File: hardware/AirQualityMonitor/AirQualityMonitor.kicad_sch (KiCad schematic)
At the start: 0 parts

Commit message: Add USB C connector with CC pulldowns and data pin pairing
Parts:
- added J1: USB_C_Receptacle_USB2.0_16P, Connector_USB:USB_C_Receptacle_HRO_TYPE-C-31-M-12, symbol Connector:USB_C_Receptacle_USB2.0_16P
- added R1, R2: 5100, Resistor_SMD:R_0603_1608Metric, symbol Device:R
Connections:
- new net: J1.B5 (CC2), R1.1
- new net: J1.A5 (CC1), R2.1
- new net: J1.A4 (VBUS), J1.A9 (VBUS), J1.B4 (VBUS), J1.B9 (VBUS)
- new net: J1.A6 (D+), J1.B6 (D+)
- new net: J1.A7 (D-), J1.B7 (D-)
- new net GND: J1.A1 (GND), J1.A12 (GND), J1.B1 (GND), J1.B12 (GND), J1.SH (SHIELD), R1.2, R2.2
- no-connect marks 0 -> 2
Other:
- title: (none) -> Air Quality Monitor

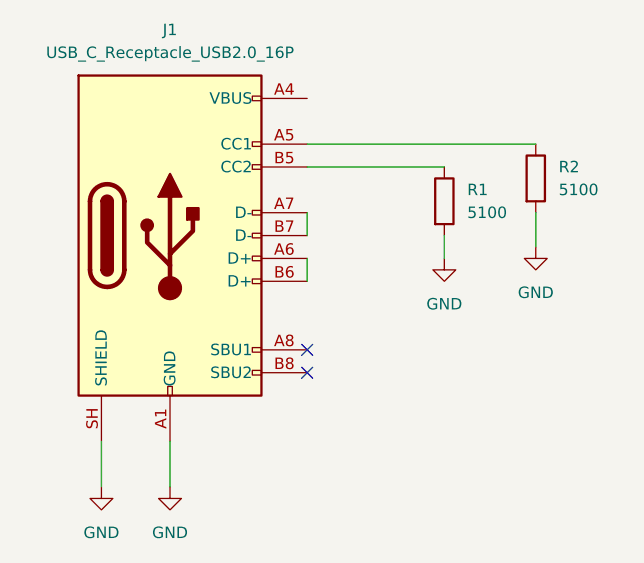
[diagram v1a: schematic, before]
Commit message: Add VBUS fuse and 5V rail
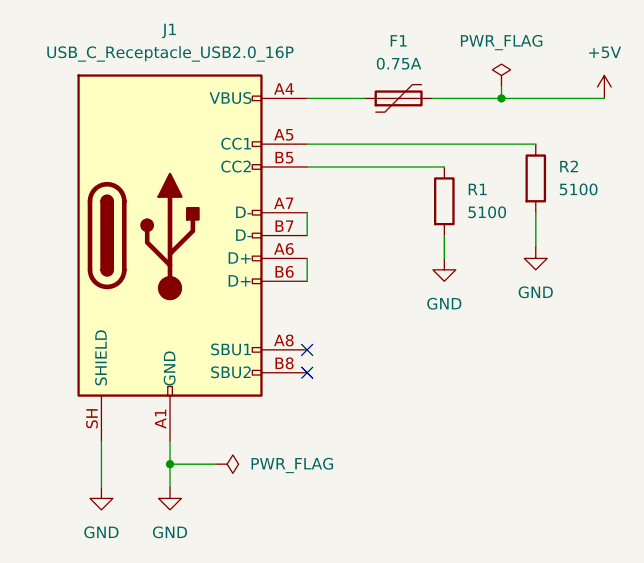
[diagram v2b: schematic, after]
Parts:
- added F1: 0.75A, Fuse:Fuse_1206_3216Metric, symbol Device:Polyfuse
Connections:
- net at J1.A4 (VBUS), J1.A9 (VBUS), J1.B4 (VBUS)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: now also F1.1
- new net +5V: F1.2

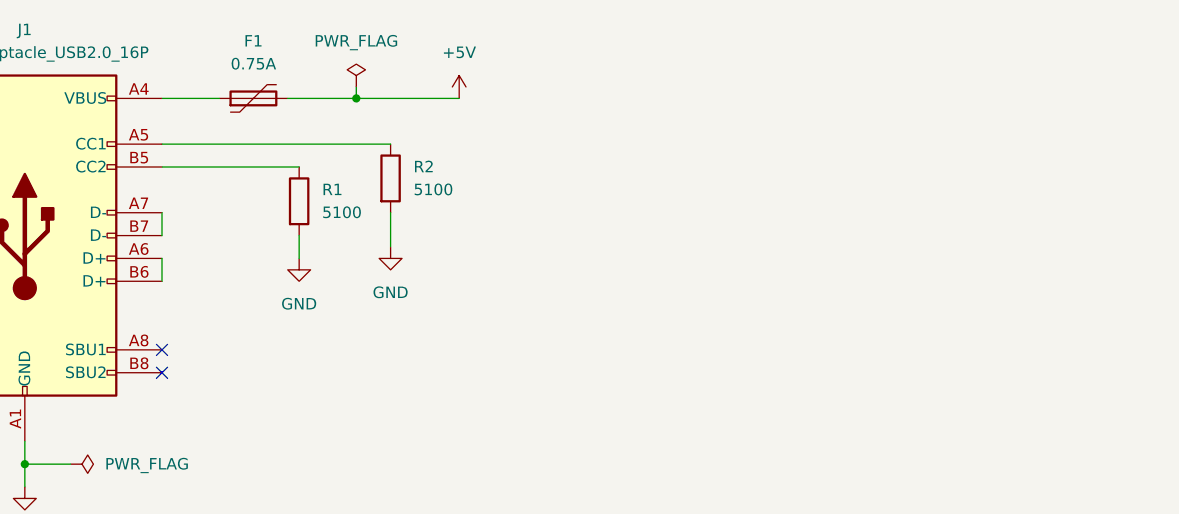
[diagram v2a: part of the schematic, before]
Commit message: Add USB ESD protection and USB data net labels
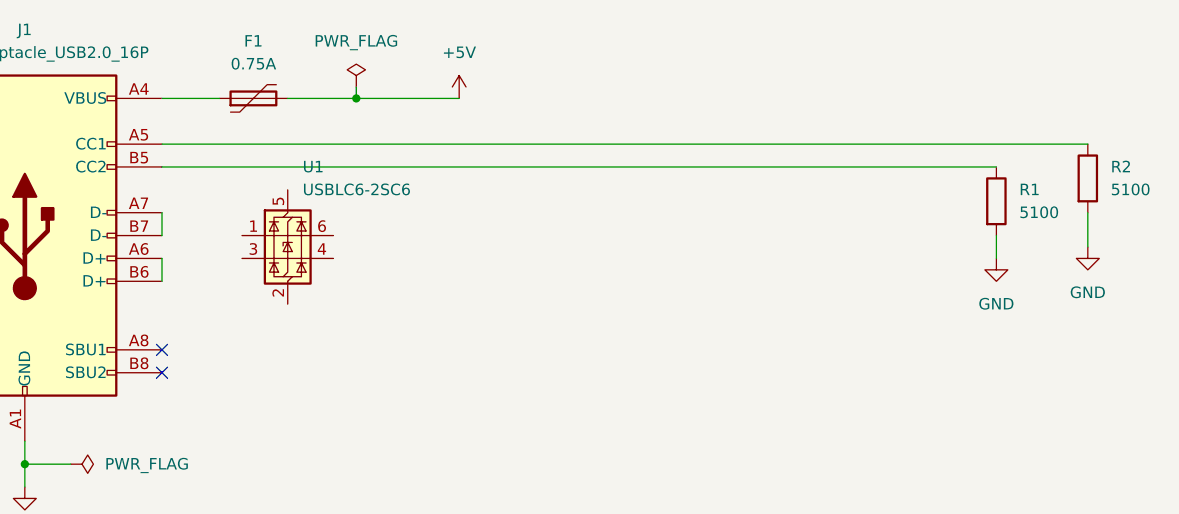
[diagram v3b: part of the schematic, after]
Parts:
- added U1: USBLC6-2SC6, Package_TO_SOT_SMD:SOT-23-6, symbol Power_Protection:USBLC6-2SC6
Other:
- moved on the sheet: R1, R2
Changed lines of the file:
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@@
 	(wire
 		(pts
-			(xy 88.9 100.33) (xy 88.9 104.14)
+			(xy 166.37 100.33) (xy 166.37 104.14)
 		)
 		(stroke
@@
 	(wire
 		(pts
-			(xy 78.74 102.87) (xy 78.74 105.41)
+			(xy 156.21 102.87) (xy 156.21 105.41)
 		)
 		(stroke
@@
 	(wire
 		(pts
-			(xy 63.5 92.71) (xy 88.9 92.71)
+			(xy 63.5 92.71) (xy 166.37 92.71)
 		)
 		(stroke
@@
 	(wire
 		(pts
-			(xy 63.5 95.25) (xy 78.74 95.25)
+			(xy 63.5 105.41) (xy 63.5 107.95)
 		)
 		(stroke
@@
 	(wire
 		(pts
-			(xy 63.5 105.41) (xy 63.5 107.95)
+			(xy 85.09 86.36) (xy 85.09 87.63)
 		)
 		(stroke
@@
 	(wire
 		(pts
-			(xy 85.09 86.36) (xy 85.09 87.63)
+			(xy 63.5 95.25) (xy 156.21 95.25)
 		)
 		(stroke
@@
 	(symbol
 		(lib_id "Device:R")
-		(at 78.74 99.06 0)
+		(at 156.21 99.06 0)
 		(unit 1)
 		(body_style 1)
@@
 		(fields_autoplaced yes)
 		(property "Reference" "R1"
-			(at 81.28 97.7899 0)
+			(at 158.75 97.7899 0)
 			(show_name no)
 			(do_not_autoplace no)
@@
 		)
 		(property "Value" "5100"
-			(at 81.28 100.3299 0)
+			(at 158.75 100.3299 0)
 			(show_name no)
 			(do_not_autoplace no)
@@
 		)
 		(property "Footprint" "Resistor_SMD:R_0603_1608Metric"
-			(at 76.962 99.06 90)
+			(at 154.432 99.06 90)
 			(hide yes)
 			(show_name no)
@@
 		)
 		(property "Datasheet" ""
-			(at 78.74 99.06 0)
+			(at 156.21 99.06 0)
 			(hide yes)
 			(show_name no)
@@
 		)
 		(property "Description" "Resistor"
-			(at 78.74 99.06 0)
+			(at 156.21 99.06 0)
 			(hide yes)
 			(show_name no)
@@
 	(symbol
 		(lib_id "power:GND")
-		(at 78.74 105.41 0)
+		(at 156.21 105.41 0)
 		(unit 1)
 		(body_style 1)
@@
 		(fields_autoplaced yes)
 		(property "Reference" "#PWR01"
-			(at 78.74 111.76 0)
+			(at 156.21 111.76 0)
 			(hide yes)
 			(show_name no)
@@
 		)
 		(property "Value" "GND"
-			(at 78.74 110.49 0)
+			(at 156.21 110.49 0)
 			(show_name no)
 			(do_not_autoplace no)
@@
 		)
 		(property "Footprint" ""
-			(at 78.74 105.41 0)
+			(at 156.21 105.41 0)
 			(hide yes)
 			(show_name no)
@@
 		)
 		(property "Datasheet" ""
-			(at 78.74 105.41 0)
+			(at 156.21 105.41 0)
 			(hide yes)
 			(show_name no)
@@
 		)
 		(property "Description" "Power symbol creates a global label with name \"GND\" , ground"
-			(at 78.74 105.41 0)
+			(at 156.21 105.41 0)
 			(hide yes)
 			(show_name no)
@@
 	(symbol
 		(lib_id "Device:R")
-		(at 88.9 96.52 0)
+		(at 166.37 96.52 0)
 		(unit 1)
 		(body_style 1)
@@
 		(fields_autoplaced yes)
 		(property "Reference" "R2"
-			(at 91.44 95.2499 0)
+			(at 168.91 95.2499 0)
 			(show_name no)
 			(do_not_autoplace no)
@@
 		)
 		(property "Value" "5100"
-			(at 91.44 97.7899 0)
+			(at 168.91 97.7899 0)
 			(show_name no)
 			(do_not_autoplace no)
@@
 		)
 		(property "Footprint" "Resistor_SMD:R_0603_1608Metric"
-			(at 87.122 96.52 90)
+			(at 164.592 96.52 90)
 			(hide yes)
 			(show_name no)
@@
 		)
 		(property "Datasheet" ""
-			(at 88.9 96.52 0)
+			(at 166.37 96.52 0)
 			(hide yes)
 			(show_name no)
@@
 		)
 		(property "Description" "Resistor"
-			(at 88.9 96.52 0)
+			(at 166.37 96.52 0)
 			(hide yes)
 			(show_name no)
@@
 	(symbol
 		(lib_id "power:GND")
-		(at 88.9 104.14 0)
+		(at 166.37 104.14 0)
 		(unit 1)
 		(body_style 1)
@@
 		(fields_autoplaced yes)
 		(property "Reference" "#PWR02"
-			(at 88.9 110.49 0)
+			(at 166.37 110.49 0)
 			(hide yes)
 			(show_name no)
@@
 		)
 		(property "Value" "GND"
-			(at 88.9 109.22 0)
+			(at 166.37 109.22 0)
 			(show_name no)
 			(do_not_autoplace no)
@@
 		)
 		(property "Footprint" ""
-			(at 88.9 104.14 0)
+			(at 166.37 104.14 0)
 			(hide yes)
 			(show_name no)
@@
 		)
 		(property "Datasheet" ""
-			(at 88.9 104.14 0)
+			(at 166.37 104.14 0)
 			(hide yes)
 			(show_name no)
@@
 		)
 		(property "Description" "Power symbol creates a global label with name \"GND\" , ground"
-			(at 88.9 104.14 0)
+			(at 166.37 104.14 0)
 			(hide yes)
 			(show_name no)
@@
 					(unit 1)
 				)
+			)
+		)
+	)
+	(symbol
+		(lib_id "Power_Protection:USBLC6-2SC6")
+		(at 77.47 102.87 0)
+		(unit 1)
+		(body_style 1)
+		(exclude_from_sim no)
+		(in_bom yes)
+		(on_board yes)
+		(in_pos_files yes)
+		(dnp no)
+		(fields_autoplaced yes)
+		(property "Reference" "U1"
+			(at 79.1211 95.25 0)
+			(show_name no)
+			(do_not_autoplace no)
+			(effects
+				(font
+					(size 1.27 1.27)
+				)
+				(justify left)
+			)
+		)
+		(property "Value" "USBLC6-2SC6"
+			(at 79.1211 97.79 0)
+			(show_name no)
+			(do_not_autoplace no)
+			(effects
+				(font
+					(size 1.27 1.27)
+				)
+				(justify left)
+			)
+		)
+		(property "Footprint" "Package_TO_SOT_SMD:SOT-23-6"
+			(at 78.74 109.22 0)
+			(hide yes)
+			(show_name no)
+			(do_not_autoplace no)
+			(effects
+				(font
+					(size 1.27 1.27)
+					(italic yes)
+				)
+				(justify left)
+			)
+		)
+		(property "Datasheet" "https://www.st.com/resource/en/datasheet/usblc6-2.pdf"
+			(at 78.74 111.125 0)
+			(hide yes)
+			(show_name no)
+			(do_not_autoplace no)
+			(effects
+				(font
+					(size 1.27 1.27)
+				)
+				(justify left)
+			)
+		)
+		(property "Description" "Very low capacitance ESD protection diode, 2 data-line, SOT-23-6"
+			(at 77.47 102.87 0)
+			(hide yes)
+			(show_name no)
+			(do_not_autoplace no)
+			(effects
+				(font
+					(size 1.27 1.27)
+				)
+			)
+		)
+		(pin "1"
+		)
+		(pin "2"
+		)
+		(pin "3"
+		)
+		(pin "4"
+		)
+		(pin "5"
+		)
+		(pin "6"
+		)
+		(instances
+			(project "AirQualityMonitor"
+				(path "/f33fd3c7-3605-4409-8b6b-4ae13c9b0ade"
+					(reference "U1")
+					(unit 1)
+				)

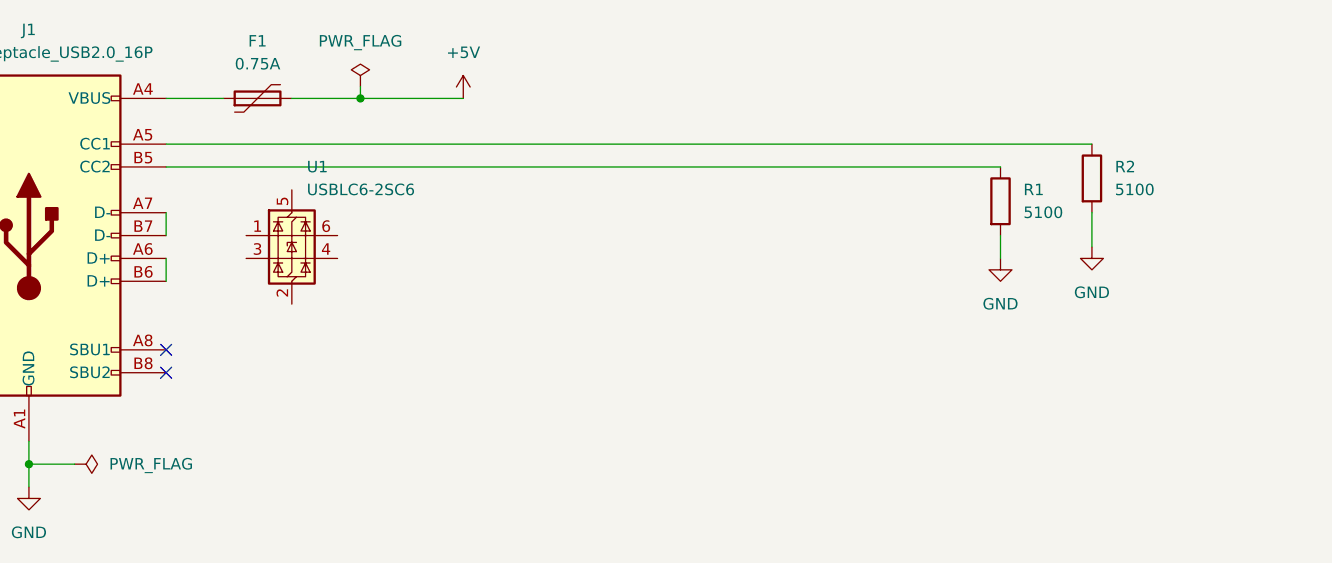
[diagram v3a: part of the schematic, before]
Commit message: Add 3.3V regulator with input and output capacitors
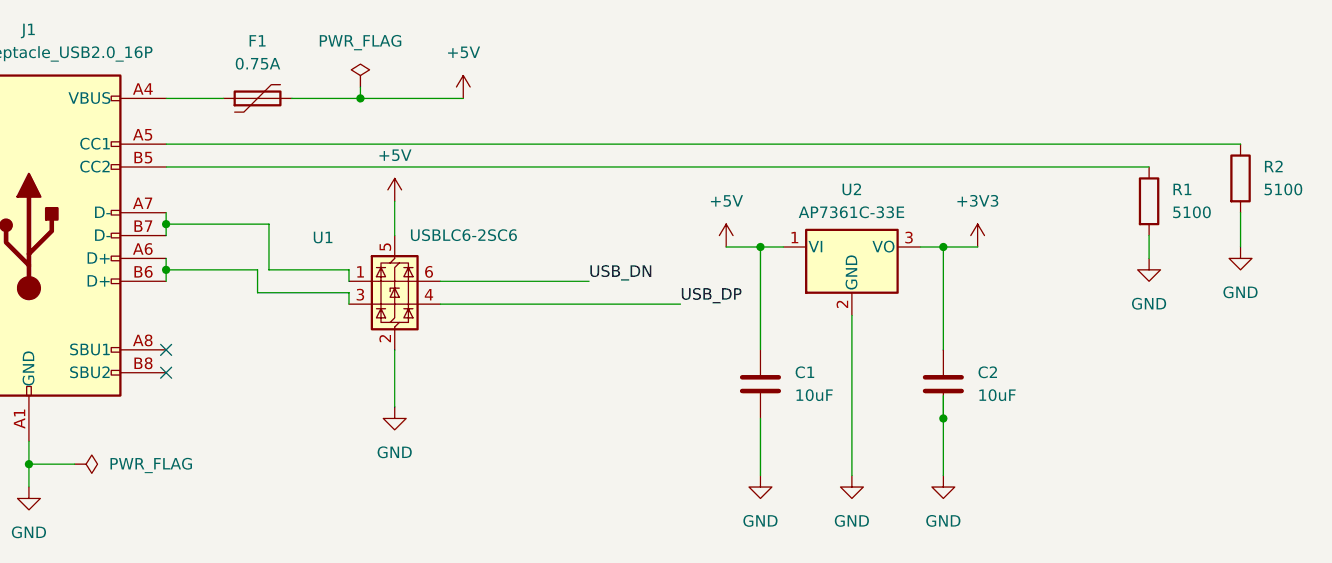
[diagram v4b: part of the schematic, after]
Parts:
- added C1, C2: 10uF, Capacitor_SMD:C_0805_2012Metric, symbol Device:C
- added U2: AP7361C-33E, Package_TO_SOT_SMD:SOT-223-3_TabPin2, symbol Regulator_Linear:AP7361C-33E
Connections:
- net +5V: now also U1.5 (VBUS), C1.1, U2.1 (VI)
- net GND: now also U1.2 (GND), C1.2, C2.2, U2.2 (GND)
- net at J1.A6 (D+), J1.B6 (D+): now also U1.3 (I/O2)
- net at J1.A7 (D-), J1.B7 (D-): now also U1.1 (I/O1)
- net USB_DP: now reaches U1.4 (I/O2)
- net USB_DN: now reaches U1.6 (I/O1)
- new net +3V3: C2.1, U2.3 (VO)
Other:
- moved on the sheet: R1, R2, U1

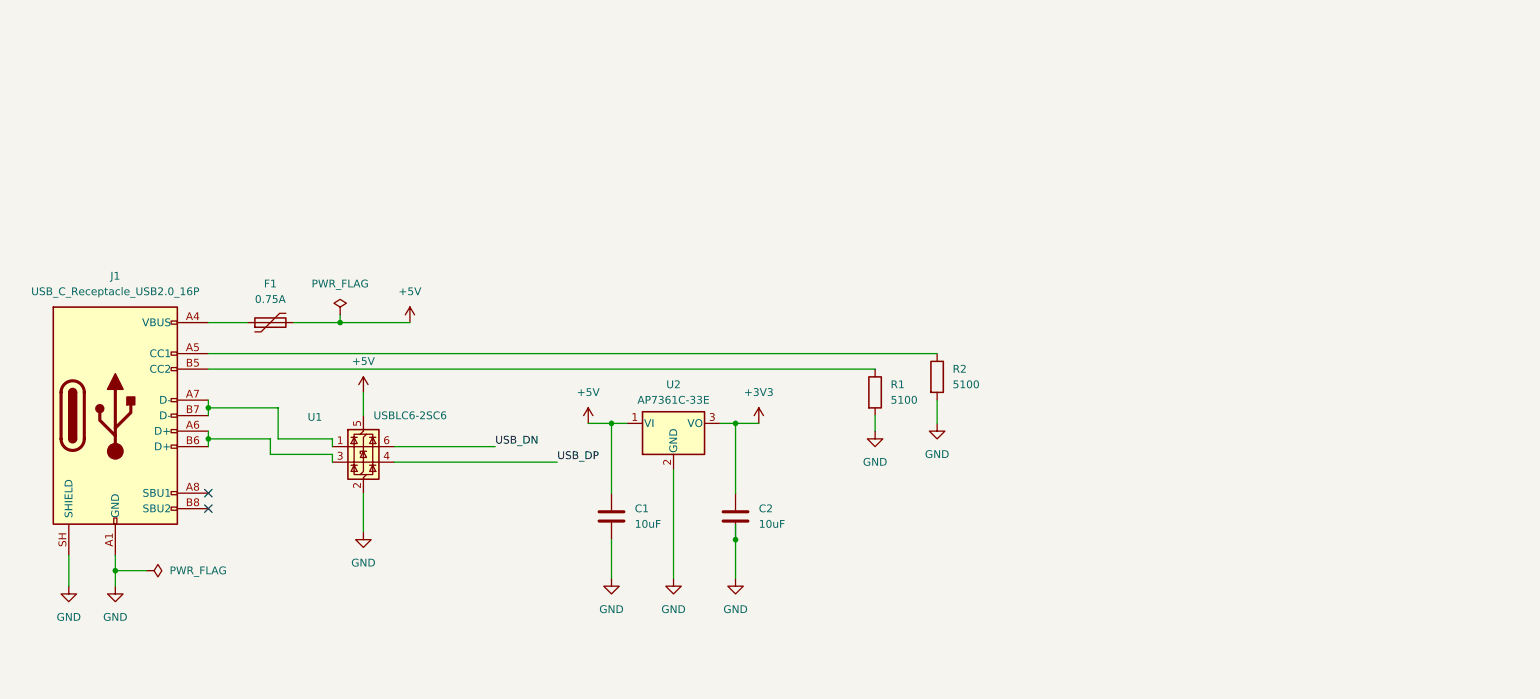
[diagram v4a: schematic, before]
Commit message: Add ESP32 S3 module with power decoupling and USB connection
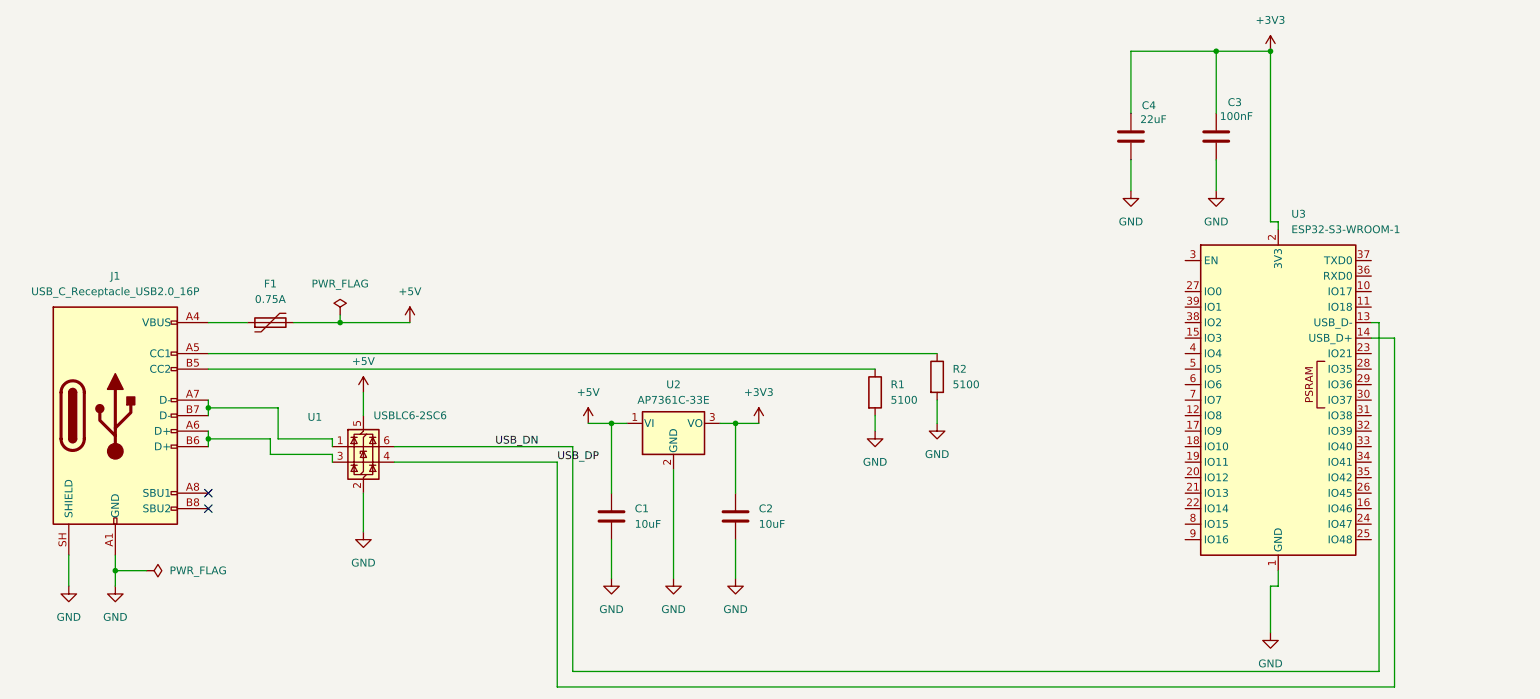
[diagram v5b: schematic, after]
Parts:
- added C3: 100nF, Capacitor_SMD:C_0805_2012Metric, symbol Device:C
- added C4: 22uF, Capacitor_SMD:C_0805_2012Metric, symbol Device:C
- added U3: ESP32-S3-WROOM-1, RF_Module:ESP32-S3-WROOM-1, symbol RF_Module:ESP32-S3-WROOM-1
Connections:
- net +3V3: now also C3.2, C4.2, U3.2 (3V3)
- net GND: now also C3.1, C4.1, U3.1 (GND), U3.40 (GND), U3.41 (GND)
- net USB_DN: now also U3.13 (USB_D-)
- net USB_DP: now also U3.14 (USB_D+)

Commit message: Add ESP32 reset and boot circuits
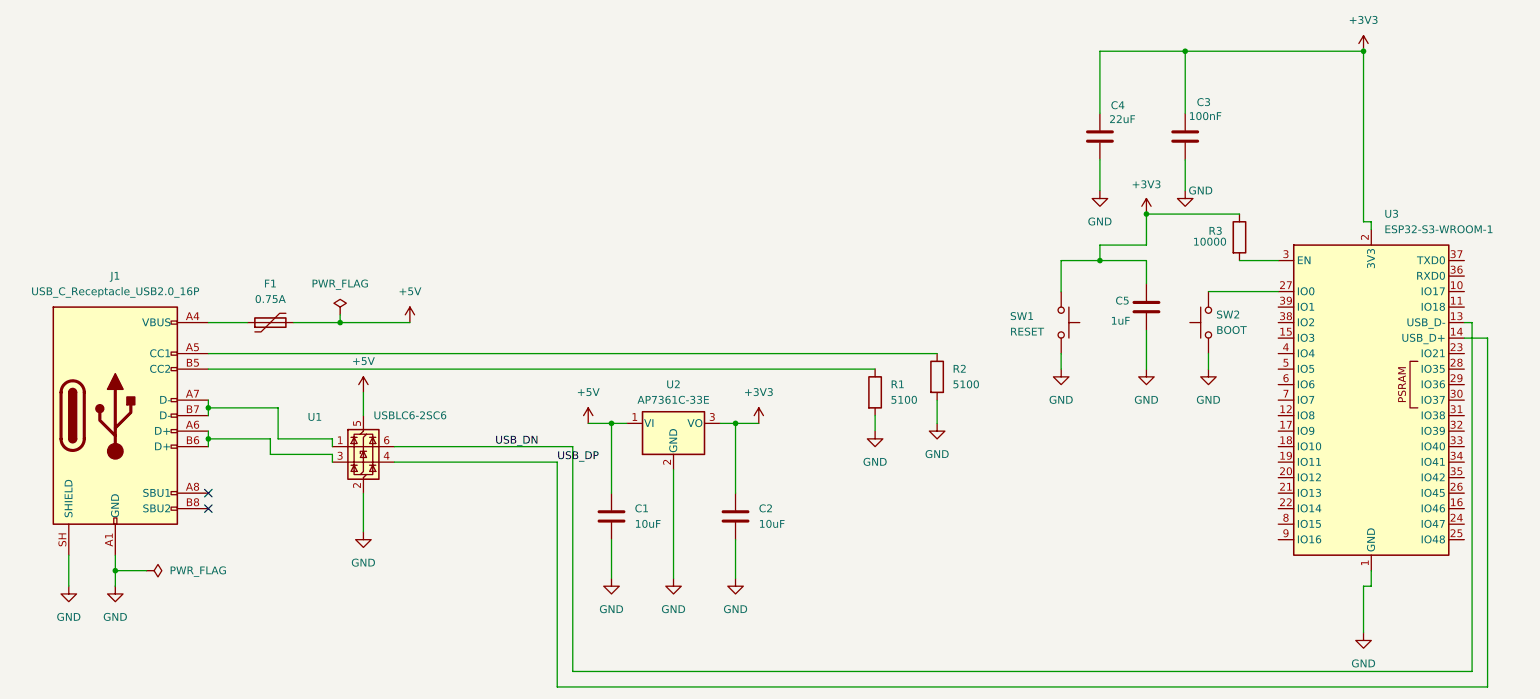
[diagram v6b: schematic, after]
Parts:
- added C5: 1uF, Capacitor_SMD:C_0603_1608Metric, symbol Device:C
- added R3: 10000, Resistor_SMD:R_0603_1608Metric, symbol Device:R
- added SW1: RESET, Button_Switch_THT:SW_PUSH_6mm, symbol Switch:SW_Push
- added SW2: BOOT, Button_Switch_THT:SW_PUSH_6mm, symbol Switch:SW_Push
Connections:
- net +3V3: now also C5.1, R3.1, SW1.1
- net GND: now also C5.2, SW1.2, SW2.1
- net at U3.27 (IO0): now also SW2.2
- net at U3.3 (EN): now also R3.2
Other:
- moved on the sheet: C3, C4, U3
